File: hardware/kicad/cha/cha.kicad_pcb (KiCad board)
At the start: 2 copper layers, 173 x 134 mm, 1 part, among them J1 AES_CHA

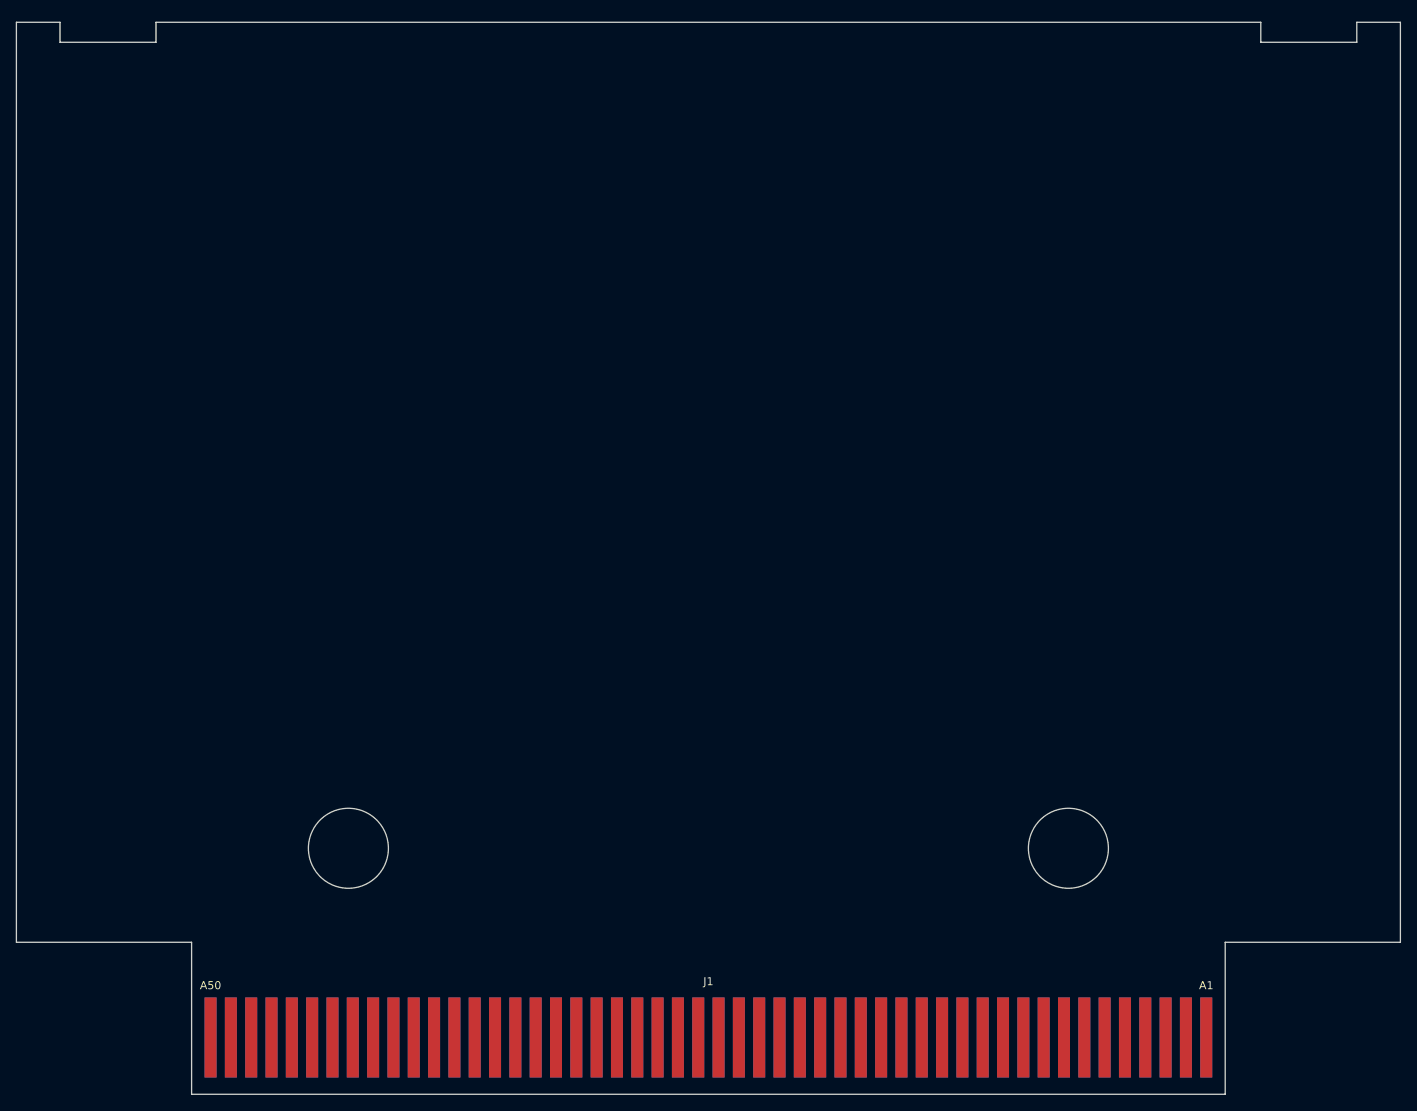
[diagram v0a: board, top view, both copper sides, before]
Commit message: Circuits imprimés 2 couches : placement et affectation des broches FPGA
- hardware/gen/pcb.py : empreintes et réseaux depuis boards.py, contour
  depuis outline.py ; ancres placées (contacts, rangée de tampons, FPGA,
  mémoires ; CHA : Pico au centre, microSD et bouton en haut), passifs
  au plus près de leur broche, masse coulée sur les deux faces.
- --pins : signaux des FPGA affectés aux broches tournées vers leur
  cible en conservant l'ordre circulaire (pins_opt.json, repris par
  fpga_pins.py) ; stable en trois passes.
- boards.py : canaux des tampons triés selon la position des contacts.
- hardware/gen/route.py : export Specctra, Freerouting, relecture de la
  session, DRC.
Placement-routage FPGA avec les nouvelles broches : en cours de
vérification.

Co-Authored-By: Claude Opus 5.5 <noreply@anthropic.com>
Claude-Session: https://claude.ai/code/session_01WKfXP1YJ8otGxZ5dsY6Agh
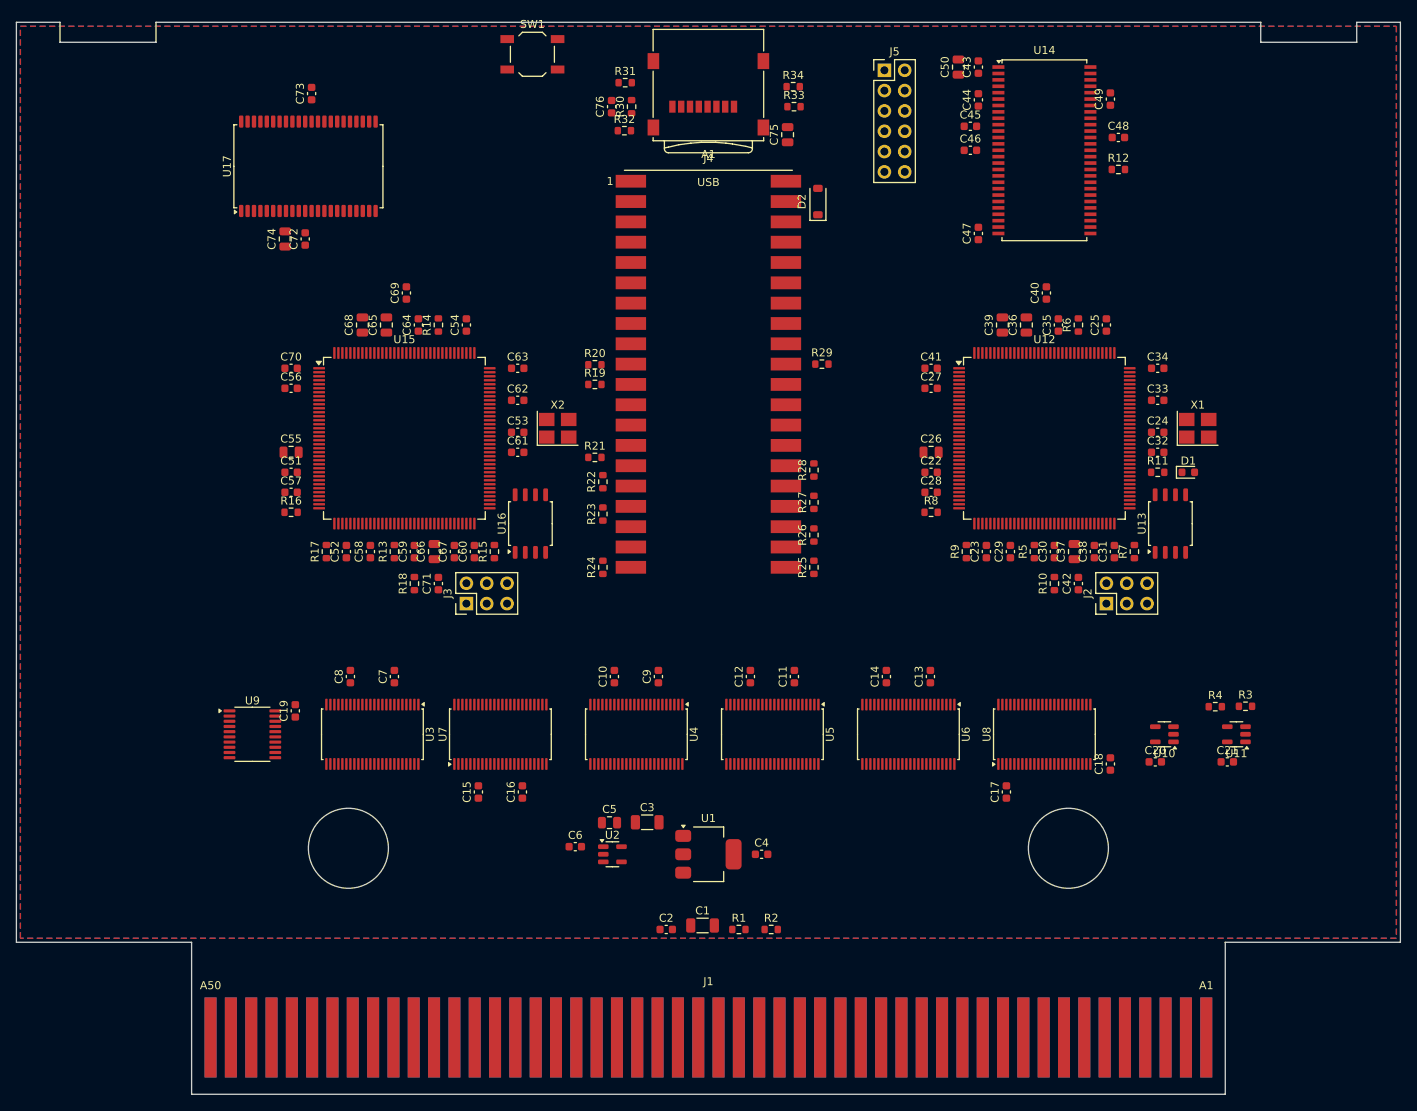
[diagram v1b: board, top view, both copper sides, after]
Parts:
- added A1: Raspberry Pi Pico 2, SDAES:RaspberryPi_Pico2_SMD, F.Cu at (150.0, 90.0)
- added C1: 22u, Capacitor_SMD:C_1206_3216Metric, F.Cu at (149.3, 158.9)
- added C10: 100n, Capacitor_SMD:C_0603_1608Metric, F.Cu at (138.2, 127.8)
- added C11: 100n, Capacitor_SMD:C_0603_1608Metric, F.Cu at (160.8, 127.8)
- added C12: 100n, Capacitor_SMD:C_0603_1608Metric, F.Cu at (155.2, 127.8)
- added C13: 100n, Capacitor_SMD:C_0603_1608Metric, F.Cu at (177.8, 127.8)
- added C14: 100n, Capacitor_SMD:C_0603_1608Metric, F.Cu at (172.2, 127.8)
- added C15: 100n, Capacitor_SMD:C_0603_1608Metric, F.Cu at (121.2, 142.2)
- added C16: 100n, Capacitor_SMD:C_0603_1608Metric, F.Cu at (126.8, 142.2)
- added C17: 100n, Capacitor_SMD:C_0603_1608Metric, F.Cu at (187.2, 142.2)
- added C18: 100n, Capacitor_SMD:C_0603_1608Metric, F.Cu at (200.2, 138.7)
- added C19: 100n, Capacitor_SMD:C_0603_1608Metric, F.Cu at (98.4, 132.1)
- added C2: 100n, Capacitor_SMD:C_0603_1608Metric, F.Cu at (144.7, 159.4)
- added C20: 100n, Capacitor_SMD:C_0603_1608Metric, F.Cu at (205.9, 138.4)
- added C21: 100n, Capacitor_SMD:C_0603_1608Metric, F.Cu at (214.9, 138.4)
- added C22: 100n, Capacitor_SMD:C_0603_1608Metric, F.Cu at (177.8, 102.2)
- added C23: 100n, Capacitor_SMD:C_0603_1608Metric, F.Cu at (184.8, 112.2)
- added C24: 100n, Capacitor_SMD:C_0603_1608Metric, F.Cu at (206.2, 97.2)
- added C25: 100n, Capacitor_SMD:C_0603_1608Metric, F.Cu at (199.8, 83.8)
- added C26: 10u, Capacitor_SMD:C_0805_2012Metric, F.Cu at (177.8, 99.8)
- added C27: 100n, Capacitor_SMD:C_0603_1608Metric, F.Cu at (177.8, 91.8)
- added C28: 100n, Capacitor_SMD:C_0603_1608Metric, F.Cu at (177.8, 104.8)
- added C29: 100n, Capacitor_SMD:C_0603_1608Metric, F.Cu at (187.8, 112.2)
- added C3: 22u, Capacitor_SMD:C_1206_3216Metric, F.Cu at (142.3, 146.0)
- added C30: 100n, Capacitor_SMD:C_0603_1608Metric, F.Cu at (193.2, 112.2)
- added C31: 100n, Capacitor_SMD:C_0603_1608Metric, F.Cu at (200.8, 112.2)
- added C32: 100n, Capacitor_SMD:C_0603_1608Metric, F.Cu at (206.2, 99.8)
- added C33: 100n, Capacitor_SMD:C_0603_1608Metric, F.Cu at (206.2, 93.2)
- added C34: 100n, Capacitor_SMD:C_0603_1608Metric, F.Cu at (206.2, 89.2)
- added C35: 100n, Capacitor_SMD:C_0603_1608Metric, F.Cu at (193.8, 83.8)
- added C36: 10u, Capacitor_SMD:C_0805_2012Metric, F.Cu at (189.8, 83.8)
- added C37: 10u, Capacitor_SMD:C_0805_2012Metric, F.Cu at (195.8, 112.2)
- added C38: 100n, Capacitor_SMD:C_0603_1608Metric, F.Cu at (198.2, 112.2)
- added C39: 10u, Capacitor_SMD:C_0805_2012Metric, F.Cu at (186.8, 83.8)
- added C4: 100n, Capacitor_SMD:C_0603_1608Metric, F.Cu at (156.7, 150.0)
- added C40: 100n, Capacitor_SMD:C_0603_1608Metric, F.Cu at (192.2, 79.8)
- added C41: 100n, Capacitor_SMD:C_0603_1608Metric, F.Cu at (177.8, 89.2)
- added C42: 100n, Capacitor_SMD:C_0603_1608Metric, F.Cu at (196.2, 116.2)
- added C43: 100n, Capacitor_SMD:C_0603_1608Metric, F.Cu at (183.8, 51.6)
- added C44: 100n, Capacitor_SMD:C_0603_1608Metric, F.Cu at (183.8, 55.7)
- added C45: 100n, Capacitor_SMD:C_0603_1608Metric, F.Cu at (182.8, 59.0)
- added C46: 100n, Capacitor_SMD:C_0603_1608Metric, F.Cu at (182.8, 62.0)
- added C47: 100n, Capacitor_SMD:C_0603_1608Metric, F.Cu at (183.8, 72.4)
- added C48: 100n, Capacitor_SMD:C_0603_1608Metric, F.Cu at (201.2, 60.4)
- added C49: 100n, Capacitor_SMD:C_0603_1608Metric, F.Cu at (200.2, 55.6)
- added C5: 10u, Capacitor_SMD:C_0805_2012Metric, F.Cu at (137.6, 146.1)
- added C50: 10u, Capacitor_SMD:C_0805_2012Metric, F.Cu at (181.2, 51.6)
- added C51: 100n, Capacitor_SMD:C_0603_1608Metric, F.Cu at (97.8, 102.2)
- added C52: 100n, Capacitor_SMD:C_0603_1608Metric, F.Cu at (104.8, 112.2)
- added C53: 100n, Capacitor_SMD:C_0603_1608Metric, F.Cu at (126.2, 97.2)
- added C54: 100n, Capacitor_SMD:C_0603_1608Metric, F.Cu at (119.8, 83.8)
- added C55: 10u, Capacitor_SMD:C_0805_2012Metric, F.Cu at (97.8, 99.8)
- added C56: 100n, Capacitor_SMD:C_0603_1608Metric, F.Cu at (97.8, 91.8)
- added C57: 100n, Capacitor_SMD:C_0603_1608Metric, F.Cu at (97.8, 104.8)
- added C58: 100n, Capacitor_SMD:C_0603_1608Metric, F.Cu at (107.8, 112.2)
- added C59: 100n, Capacitor_SMD:C_0603_1608Metric, F.Cu at (113.2, 112.2)
- added C6: 1u, Capacitor_SMD:C_0603_1608Metric, F.Cu at (133.4, 149.1)
- added C60: 100n, Capacitor_SMD:C_0603_1608Metric, F.Cu at (120.8, 112.2)
- added C61: 100n, Capacitor_SMD:C_0603_1608Metric, F.Cu at (126.2, 99.8)
- added C62: 100n, Capacitor_SMD:C_0603_1608Metric, F.Cu at (126.2, 93.2)
- added C63: 100n, Capacitor_SMD:C_0603_1608Metric, F.Cu at (126.2, 89.2)
- added C64: 100n, Capacitor_SMD:C_0603_1608Metric, F.Cu at (113.8, 83.8)
- added C65: 10u, Capacitor_SMD:C_0805_2012Metric, F.Cu at (109.8, 83.8)
- added C66: 10u, Capacitor_SMD:C_0805_2012Metric, F.Cu at (115.8, 112.2)
- added C67: 100n, Capacitor_SMD:C_0603_1608Metric, F.Cu at (118.2, 112.2)
- added C68: 10u, Capacitor_SMD:C_0805_2012Metric, F.Cu at (106.8, 83.8)
- added C69: 100n, Capacitor_SMD:C_0603_1608Metric, F.Cu at (112.2, 79.8)
- added C7: 100n, Capacitor_SMD:C_0603_1608Metric, F.Cu at (110.8, 127.8)
- added C70: 100n, Capacitor_SMD:C_0603_1608Metric, F.Cu at (97.8, 89.2)
- added C71: 100n, Capacitor_SMD:C_0603_1608Metric, F.Cu at (116.2, 116.2)
- added C72: 100n, Capacitor_SMD:C_0603_1608Metric, F.Cu at (99.6, 73.1)
- added C73: 100n, Capacitor_SMD:C_0603_1608Metric, F.Cu at (100.4, 54.9)
- added C74: 10u, Capacitor_SMD:C_0805_2012Metric, F.Cu at (97.1, 73.1)
- added C75: 10u, Capacitor_SMD:C_0805_2012Metric, F.Cu at (159.9, 60.0)
- added C76: 100n, Capacitor_SMD:C_0603_1608Metric, F.Cu at (137.9, 56.5)
- added C8: 100n, Capacitor_SMD:C_0603_1608Metric, F.Cu at (105.2, 127.8)
- added C9: 100n, Capacitor_SMD:C_0603_1608Metric, F.Cu at (143.8, 127.8)
- added D1: LED, LED_SMD:LED_0603_1608Metric, F.Cu at (210.0, 102.2)
- added D2: SS14 / BAT60A, Diode_SMD:D_SOD-123, F.Cu at (163.7, 68.4)
- added J2: PROG C, Connector_PinHeader_2.54mm:PinHeader_2x03_P2.54mm_Vertical, F.Cu at (199.8, 118.7)
- added J3: PROG SM, Connector_PinHeader_2.54mm:PinHeader_2x03_P2.54mm_Vertical, F.Cu at (119.8, 118.7)
- added J4: microSD, Connector_Card:microSD_HC_Wuerth_693072010801, F.Cu at (150.0, 55.0)
- added J5: Câble PROG-CHA, Connector_PinHeader_2.54mm:PinHeader_2x06_P2.54mm_Vertical, F.Cu at (172.0, 52.0)
- added R1: 0, Resistor_SMD:R_0603_1608Metric, F.Cu at (153.8, 159.4)
- added R10: 10k, Resistor_SMD:R_0603_1608Metric, F.Cu at (193.2, 116.2)
- added R11: 470, Resistor_SMD:R_0603_1608Metric, F.Cu at (206.2, 102.2)
- added R12: 33, Resistor_SMD:R_0603_1608Metric, F.Cu at (201.2, 64.4)
- added R13: 100, Resistor_SMD:R_0603_1608Metric, F.Cu at (110.8, 112.2)
- added R14: 100, Resistor_SMD:R_0603_1608Metric, F.Cu at (116.2, 83.8)
- added R15: 10k, Resistor_SMD:R_0603_1608Metric, F.Cu at (123.2, 112.2)
- added R16: 10k, Resistor_SMD:R_0603_1608Metric, F.Cu at (97.8, 107.2)
- added R17: 10k, Resistor_SMD:R_0603_1608Metric, F.Cu at (102.2, 112.2)
- added R18: 10k, Resistor_SMD:R_0603_1608Metric, F.Cu at (113.2, 116.2)
- added R19: 33, Resistor_SMD:R_0603_1608Metric, F.Cu at (135.8, 91.3)
- added R2: 0, Resistor_SMD:R_0603_1608Metric, F.Cu at (157.8, 159.4)
- added R20: 33, Resistor_SMD:R_0603_1608Metric, F.Cu at (135.8, 88.8)
- added R21: 33, Resistor_SMD:R_0603_1608Metric, F.Cu at (135.8, 100.4)
- added R22: 33, Resistor_SMD:R_0603_1608Metric, F.Cu at (136.8, 103.4)
- added R23: 33, Resistor_SMD:R_0603_1608Metric, F.Cu at (136.8, 107.5)
- added R24: 33, Resistor_SMD:R_0603_1608Metric, F.Cu at (136.8, 114.1)
- added R25: 33, Resistor_SMD:R_0603_1608Metric, F.Cu at (163.2, 114.1)
- added R26: 33, Resistor_SMD:R_0603_1608Metric, F.Cu at (163.2, 110.1)
- added R27: 33, Resistor_SMD:R_0603_1608Metric, F.Cu at (163.2, 106.0)
- added R28: 33, Resistor_SMD:R_0603_1608Metric, F.Cu at (163.2, 102.0)
- added R29: 10k, Resistor_SMD:R_0603_1608Metric, F.Cu at (164.2, 88.7)
- added R3: 10k, Resistor_SMD:R_0603_1608Metric, F.Cu at (217.1, 131.5)
- added R30: 10k, Resistor_SMD:R_0603_1608Metric, F.Cu at (140.4, 56.5)
- added R31: 10k, Resistor_SMD:R_0603_1608Metric, F.Cu at (139.6, 53.5)
- added R32: 10k, Resistor_SMD:R_0603_1608Metric, F.Cu at (139.5, 59.5)
- added R33: 10k, Resistor_SMD:R_0603_1608Metric, F.Cu at (160.7, 56.5)
- added R34: 10k, Resistor_SMD:R_0603_1608Metric, F.Cu at (160.6, 54.0)
- added R4: 10k, Resistor_SMD:R_0603_1608Metric, F.Cu at (213.4, 131.6)
- added R5: 100, Resistor_SMD:R_0603_1608Metric, F.Cu at (190.8, 112.2)
- added R6: 100, Resistor_SMD:R_0603_1608Metric, F.Cu at (196.2, 83.8)
- added R7: 10k, Resistor_SMD:R_0603_1608Metric, F.Cu at (203.2, 112.2)
- added R8: 10k, Resistor_SMD:R_0603_1608Metric, F.Cu at (177.8, 107.2)
- added R9: 10k, Resistor_SMD:R_0603_1608Metric, F.Cu at (182.2, 112.2)
- added SW1: Retour menu, Button_Switch_SMD:SW_SPST_TL3342, F.Cu at (128.0, 50.0)
- added U1: AMS1117-3.3, Package_TO_SOT_SMD:SOT-223-3_TabPin2, F.Cu at (150.0, 150.0)
- added U10: 74AHCT1G32, Package_TO_SOT_SMD:SOT-23-5, F.Cu at (207.0, 135.0)
- added U11: 74LVC1G07, Package_TO_SOT_SMD:SOT-23-5, F.Cu at (216.0, 135.0)
- added U12: iCE40HX4K-TQ144, Package_QFP:TQFP-144_20x20mm_P0.5mm, F.Cu at (192.0, 98.0)
- added U13: W25Q32JVSS, Package_SO:SOIC-8_5.23x5.23mm_P1.27mm, F.Cu at (207.8, 108.7)
- added U14: AS4C32M16SB-6TIN, Package_SO:TSOP-II-54_22.2x10.16mm_P0.8mm, F.Cu at (192.0, 62.0)
- added U15: iCE40HX4K-TQ144, Package_QFP:TQFP-144_20x20mm_P0.5mm, F.Cu at (112.0, 98.0)
- added U16: W25Q32JVSS, Package_SO:SOIC-8_5.23x5.23mm_P1.27mm, F.Cu at (127.8, 108.7)
- added U17: IS61WV10248EDBLL-10TLI, Package_SO:TSOP-II-44_10.16x18.41mm_P0.8mm, F.Cu at (100.0, 64.0)
- added U2: AP2112K-1.2, Package_TO_SOT_SMD:SOT-23-5, F.Cu at (138.0, 150.0)
- added U3: 74LVC16244A, Package_SO:TSSOP-48_6.1x12.5mm_P0.5mm, F.Cu at (108.0, 135.0)
- added U4: 74LVC16244A, Package_SO:TSSOP-48_6.1x12.5mm_P0.5mm, F.Cu at (141.0, 135.0)
- added U5: 74LVC16244A, Package_SO:TSSOP-48_6.1x12.5mm_P0.5mm, F.Cu at (158.0, 135.0)
- added U6: 74LVC16244A, Package_SO:TSSOP-48_6.1x12.5mm_P0.5mm, F.Cu at (175.0, 135.0)
- added U7: 74AHCT16244, Package_SO:TSSOP-48_6.1x12.5mm_P0.5mm, F.Cu at (124.0, 135.0)
- added U8: 74AHCT16244, Package_SO:TSSOP-48_6.1x12.5mm_P0.5mm, F.Cu at (192.0, 135.0)
- added U9: 74AHCT244, Package_SO:TSSOP-20_4.4x6.5mm_P0.65mm, F.Cu at (93.0, 135.0)
- added X1: 25 MHz 3,3 V, Oscillator:Oscillator_SMD_Abracon_ASE-4Pin_3.2x2.5mm_HandSoldering, F.Cu at (211.2, 96.8)
- added X2: 25 MHz 3,3 V, Oscillator:Oscillator_SMD_Abracon_ASE-4Pin_3.2x2.5mm_HandSoldering, F.Cu at (131.2, 96.8)
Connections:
- J1 pad B1: (no net) -> GND
- J1 pad B10: (no net) -> AES_FIXD7
- J1 pad B11: (no net) -> AES_P1
- J1 pad B12: (no net) -> AES_P3
- J1 pad B13: (no net) -> AES_P5
- J1 pad B14: (no net) -> AES_P7
- J1 pad B15: (no net) -> AES_P9
- J1 pad B16: (no net) -> AES_P11
- J1 pad B17: (no net) -> AES_P13
- J1 pad B18: (no net) -> AES_P15
- J1 pad B19: (no net) -> AES_P17
- J1 pad B2: (no net) -> GND
- J1 pad B20: (no net) -> AES_P19
- J1 pad B21: (no net) -> AES_P21
- J1 pad B22: (no net) -> AES_P23
- J1 pad B23: (no net) -> AES_R_OUT
- J1 pad B24: (no net) -> AES_R_IN
- J1 pad B25: (no net) -> +5V
- J1 pad B26: (no net) -> +5V
- J1 pad B27: (no net) -> +5V
- J1 pad B3: (no net) -> AES_FIXD0
- J1 pad B30: (no net) -> AES_DOTA
- J1 pad B31: (no net) -> AES_DOTB
- J1 pad B32: (no net) -> AES_GAD0
- J1 pad B33: (no net) -> AES_GAD1
- J1 pad B34: (no net) -> AES_GAD2
- J1 pad B35: (no net) -> AES_GAD3
- J1 pad B36: (no net) -> AES_GBD0
- J1 pad B37: (no net) -> AES_GBD1
- J1 pad B38: (no net) -> AES_GBD2
- J1 pad B39: (no net) -> AES_GBD3
- J1 pad B4: (no net) -> AES_FIXD1
- J1 pad B40: (no net) -> AES_SDD0
- J1 pad B41: (no net) -> AES_SDD1
- J1 pad B42: (no net) -> AES_SDD2
- J1 pad B43: (no net) -> AES_SDD3
- J1 pad B44: (no net) -> AES_SDD4
- J1 pad B45: (no net) -> AES_SDD5
- J1 pad B46: (no net) -> AES_SDD6
- J1 pad B47: (no net) -> AES_SDD7
- J1 pad B49: (no net) -> GND
- J1 pad B5: (no net) -> AES_FIXD2
- J1 pad B50: (no net) -> GND
- J1 pad B6: (no net) -> AES_FIXD3
- J1 pad B7: (no net) -> AES_FIXD4
- J1 pad B8: (no net) -> AES_FIXD5
- J1 pad B9: (no net) -> AES_FIXD6
- J1 pad T1: (no net) -> GND
- J1 pad T10: (no net) -> AES_CA4
- J1 pad T11: (no net) -> AES_P0
- J1 pad T12: (no net) -> AES_P2
- J1 pad T13: (no net) -> AES_P4
- J1 pad T14: (no net) -> AES_P6
- J1 pad T15: (no net) -> AES_P8
- J1 pad T16: (no net) -> AES_P10
- J1 pad T17: (no net) -> AES_P12
- J1 pad T18: (no net) -> AES_P14
- J1 pad T19: (no net) -> AES_P16
- J1 pad T2: (no net) -> GND
- J1 pad T20: (no net) -> AES_P18
- J1 pad T21: (no net) -> AES_P20
- J1 pad T22: (no net) -> AES_P22
- J1 pad T23: (no net) -> AES_L_OUT
- J1 pad T24: (no net) -> AES_L_IN
- J1 pad T25: (no net) -> +5V
- J1 pad T26: (no net) -> +5V
- J1 pad T27: (no net) -> +5V
- J1 pad T28: (no net) -> AES_SDRD0
- J1 pad T3: (no net) -> AES_PCK1B
- J1 pad T30: (no net) -> AES_SDA0
- J1 pad T31: (no net) -> AES_SDA1
- J1 pad T32: (no net) -> AES_SDA2
- J1 pad T33: (no net) -> AES_SDA3
- J1 pad T34: (no net) -> AES_SDA4
- J1 pad T35: (no net) -> AES_SDA5
- J1 pad T36: (no net) -> AES_SDA6
- J1 pad T37: (no net) -> AES_SDA7
- J1 pad T38: (no net) -> AES_SDA8
- J1 pad T39: (no net) -> AES_SDA9
- J1 pad T4: (no net) -> AES_PCK2B
- J1 pad T40: (no net) -> AES_SDA10
- J1 pad T41: (no net) -> AES_SDA11
- J1 pad T42: (no net) -> AES_SDA12
- J1 pad T43: (no net) -> AES_SDA13
- J1 pad T44: (no net) -> AES_SDA14
- J1 pad T45: (no net) -> AES_SDA15
- J1 pad T46: (no net) -> AES_SDMRD
- J1 pad T47: (no net) -> AES_SDROM
- J1 pad T49: (no net) -> GND
- J1 pad T5: (no net) -> AES_12M
- J1 pad T50: (no net) -> GND
- J1 pad T6: (no net) -> AES_2H1
- J1 pad T7: (no net) -> AES_EVEN
- J1 pad T8: (no net) -> AES_H
- J1 pad T9: (no net) -> AES_LOAD
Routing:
- added copper zone on B.Cu, net GND
- added copper zone on F.Cu, net GND

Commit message: Circuits imprimés en 4 couches
Empilement F.Cu signaux / In1 masse / In2 +3V3 / B.Cu signaux : chemin
de retour continu pour la SDRAM à 100 MHz et découplage des FPGA.
route.py déclare les couches internes « power » pour Freerouting.
Doc : fréquences des FPGA avec les broches du circuit imprimé (P à
100,2 MHz, limite).

Co-Authored-By: Claude Opus 5.5 <noreply@anthropic.com>
Claude-Session: https://claude.ai/code/session_01WKfXP1YJ8otGxZ5dsY6Agh
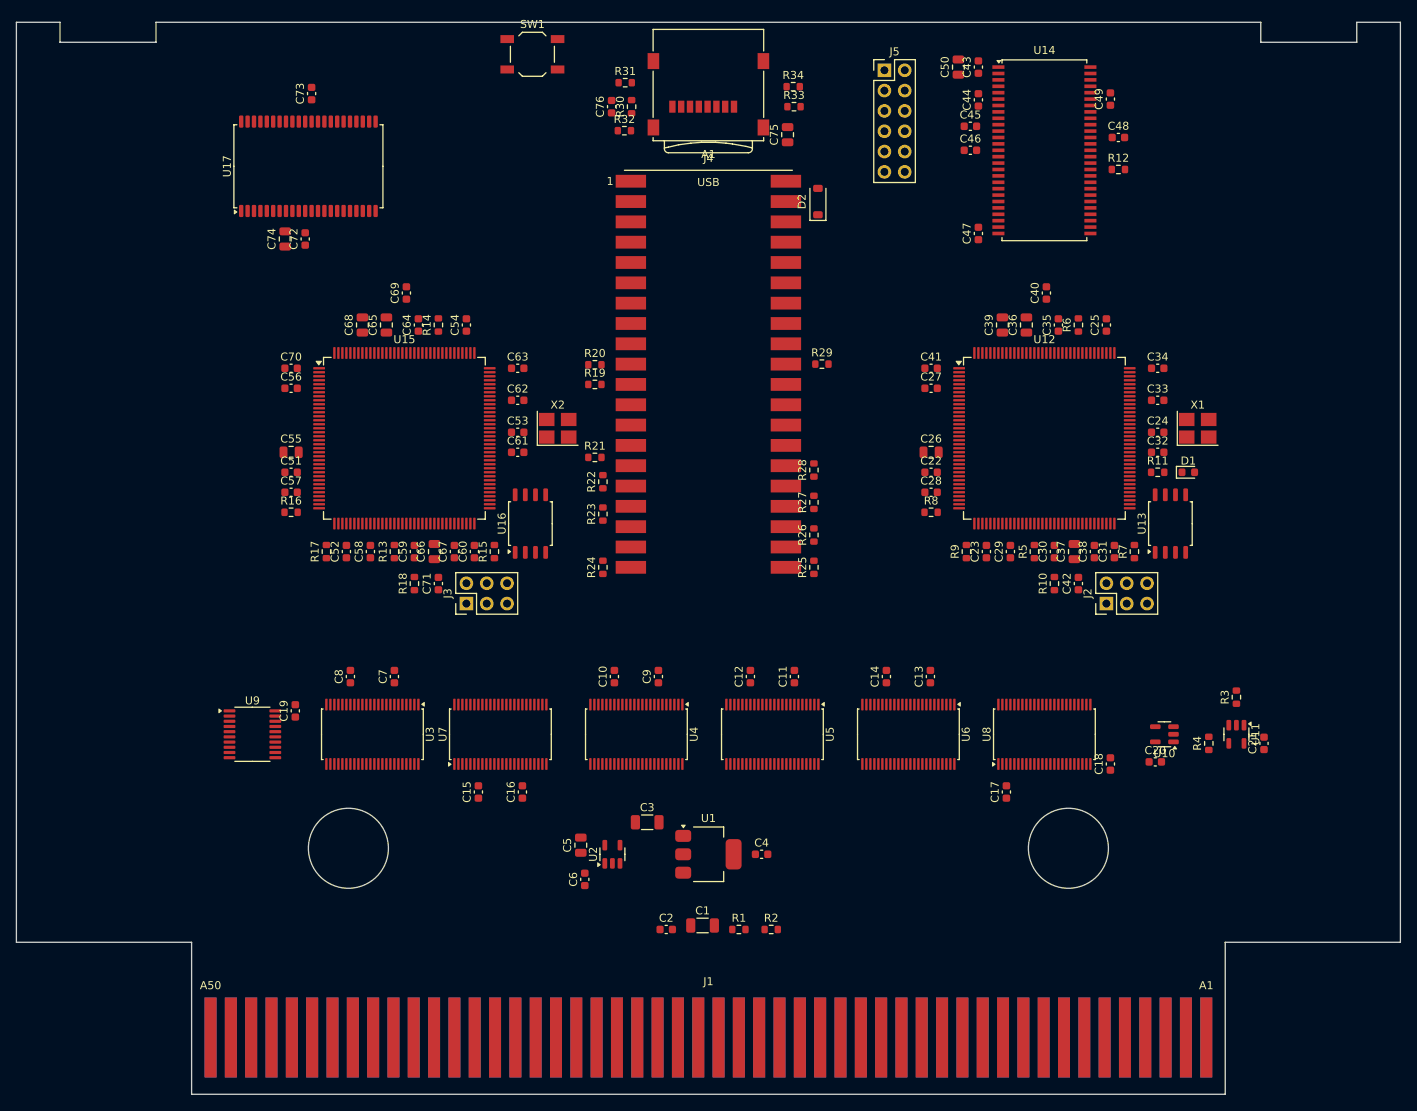
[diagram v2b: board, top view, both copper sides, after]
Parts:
- moved C21 5.14 mm to (219.4, 136.1), turned to 90 degrees
- moved R4 4.66 mm to (212.6, 136.1), turned to 90 degrees
- moved C5 4.56 mm to (134.1, 148.9), turned to 90 degrees
- moved C6 4.26 mm to (134.6, 153.1), turned to 90 degrees
- moved R3 1.61 mm to (216.0, 130.4), turned to 90 degrees
- turned U11 to -90 degrees
- turned U2 to 90 degrees
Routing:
- added copper zone on In2.Cu, net +3V3
- added copper zone on In1.Cu, net GND
- removed copper zone on B.Cu, net GND
- removed copper zone on F.Cu, net GND
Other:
- copper layers 2 -> 4

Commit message: PCB : découplage sous les boîtiers, en face arrière
Les condensateurs de découplage des FPGA, mémoires et tampons, placés
devant les rangées de broches, bloquaient leur sortie (premier essai
de routage : 52 % des broches sorties, 116 liaisons non routées). Ils
sont désormais sous le boîtier, face arrière, reliés aux plans par
des vias courts.

Co-Authored-By: Claude Opus 5.5 <noreply@anthropic.com>
Claude-Session: https://claude.ai/code/session_01WKfXP1YJ8otGxZ5dsY6Agh
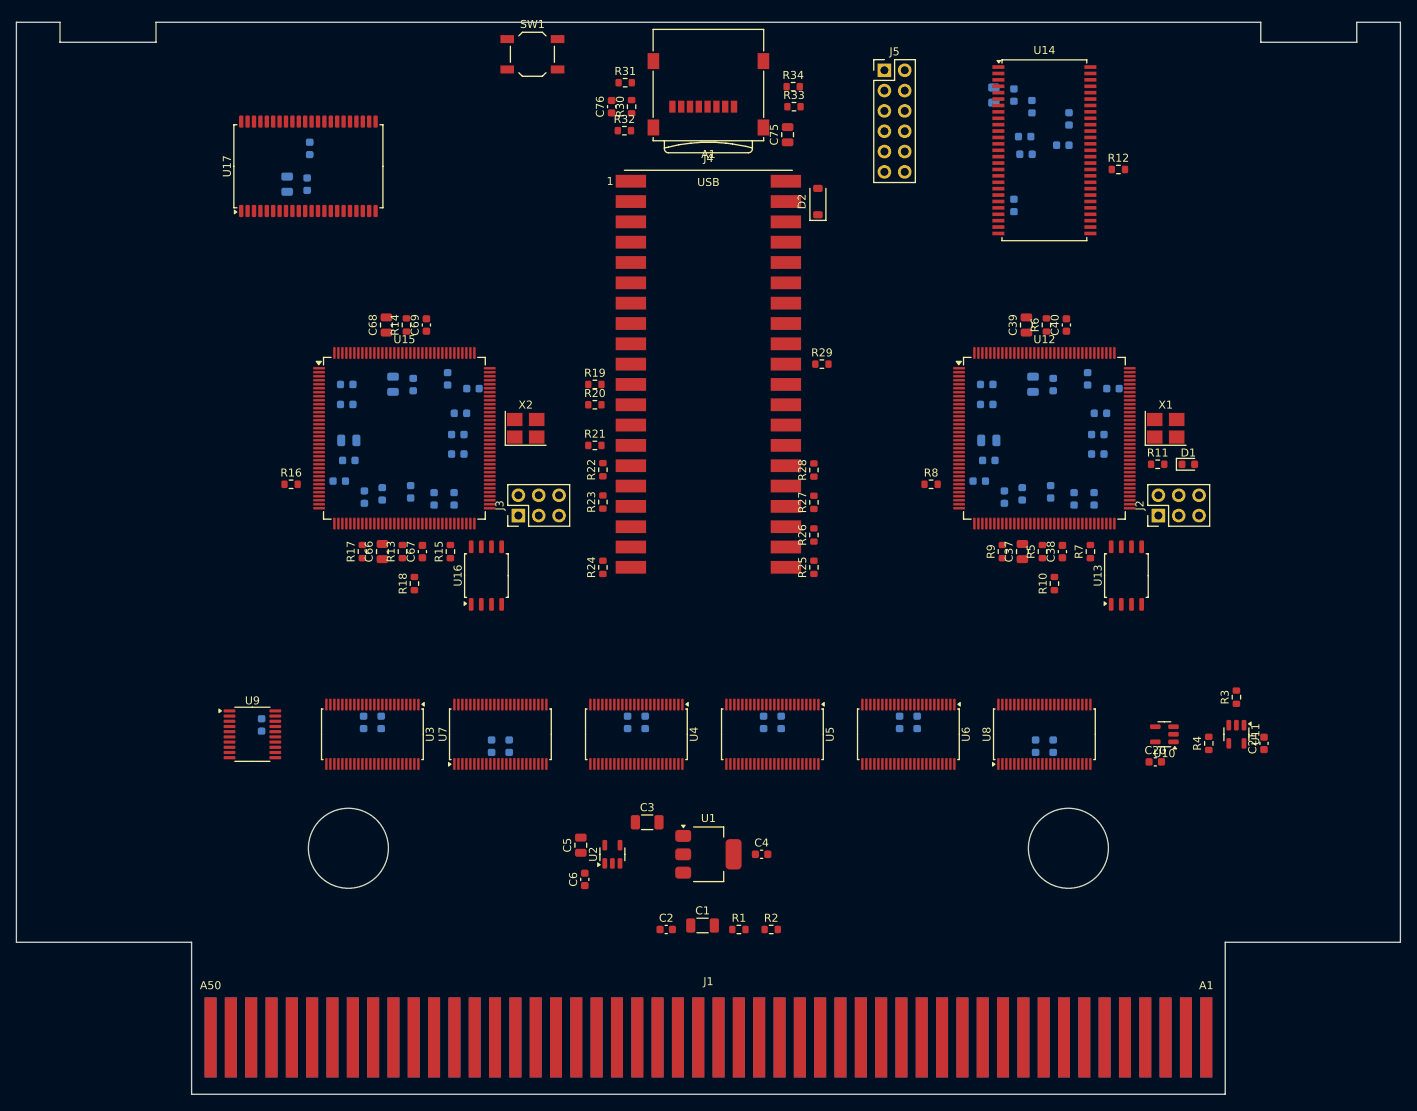
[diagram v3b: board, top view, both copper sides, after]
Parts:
- C10, C11, C12, C13, C14, C15, C16, C17, C18, C19, C22, C23, C24, C25, C26, C27, C28, C29, C30, C31, C32, C33, C34, C35, C36, C41, C42, C43, C44, C45, C46, C47, C48, C49, C50, C51, C52, C53, C54, C55, C56, C57, C58, C59, C60, C61, C62, C63, C64, C65, C7, C70, C71, C72, C73, C74, C8, C9: moved to B.Cu
- moved J2 12.8 mm to (206.2, 107.7)
- moved J3 12.8 mm to (126.2, 107.7)
- moved C42 10.6 mm to (195.7, 105.6), turned to -90 degrees
- moved C71 10.6 mm to (115.7, 105.6), turned to -90 degrees
- moved U13 8.51 mm to (202.2, 115.2)
- moved U16 8.51 mm to (122.2, 115.2)
- moved C24 7.50 mm to (198.7, 97.5)
- moved C53 7.50 mm to (118.7, 97.5)
- moved C32 7.49 mm to (198.7, 100.0)
- moved C61 7.49 mm to (118.7, 100.0)
- moved C18 7.49 mm to (193.1, 136.5), turned to -90 degrees
- moved C30 7.49 mm to (192.8, 104.7), turned to -90 degrees
- moved C59 7.49 mm to (112.8, 104.7), turned to -90 degrees
- moved C35 7.48 mm to (193.1, 91.3), turned to -90 degrees
- moved C64 7.48 mm to (113.1, 91.3), turned to -90 degrees
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
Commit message: PCB CHA : ouverture du lecteur microSD tournée vers le bord supérieur
Co-Authored-By: Claude Opus 5.5 <noreply@anthropic.com>
Claude-Session: https://claude.ai/code/session_01WKfXP1YJ8otGxZ5dsY6Agh
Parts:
- moved R33 21.6 mm to (139.3, 53.5)
- moved R34 21.4 mm to (139.4, 51.0)
- moved R32 21.0 mm to (160.5, 59.0)
- moved R31 21.0 mm to (160.4, 56.5)
- moved C75 20.0 mm to (140.1, 57.0)
- moved R30 19.4 mm to (159.6, 53.5)
- moved C76 4.92 mm to (140.1, 61.0)
- turned J4 to 0 degrees
